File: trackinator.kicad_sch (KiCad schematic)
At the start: 2 parts, among them U6 FE2.1

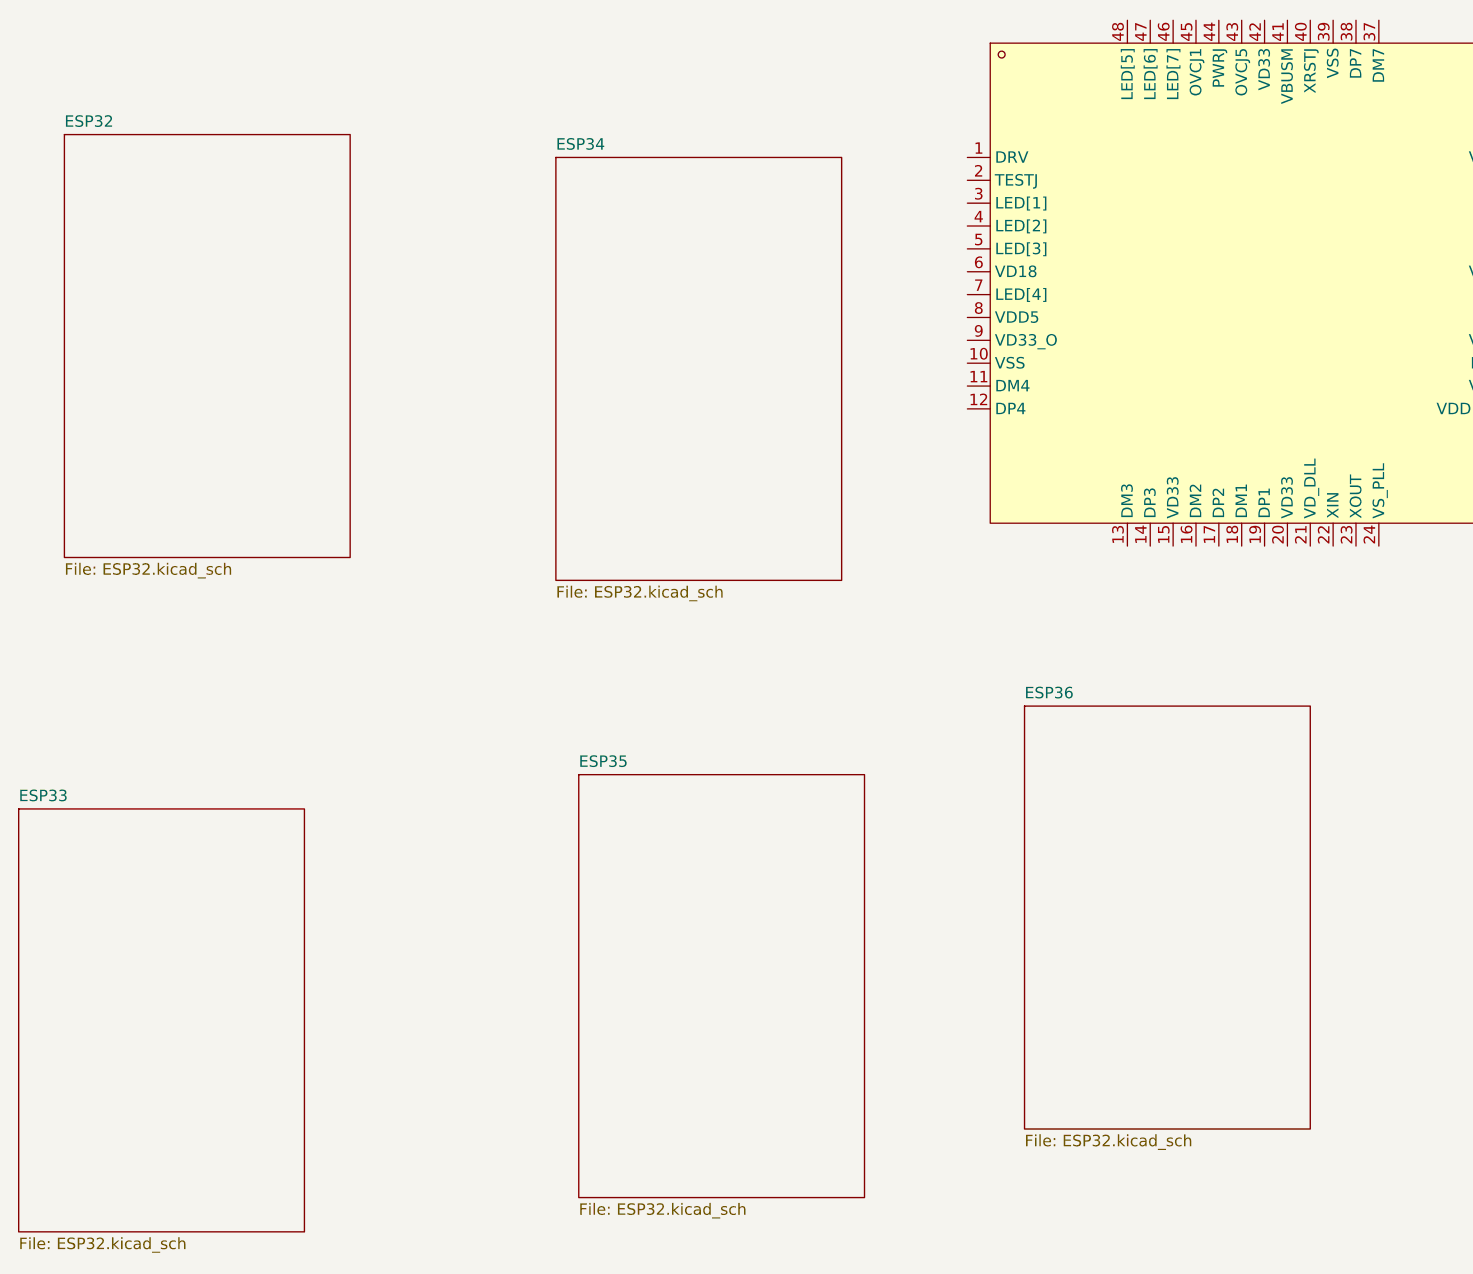
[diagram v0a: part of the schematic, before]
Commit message: FFC camera connector + pin mapping
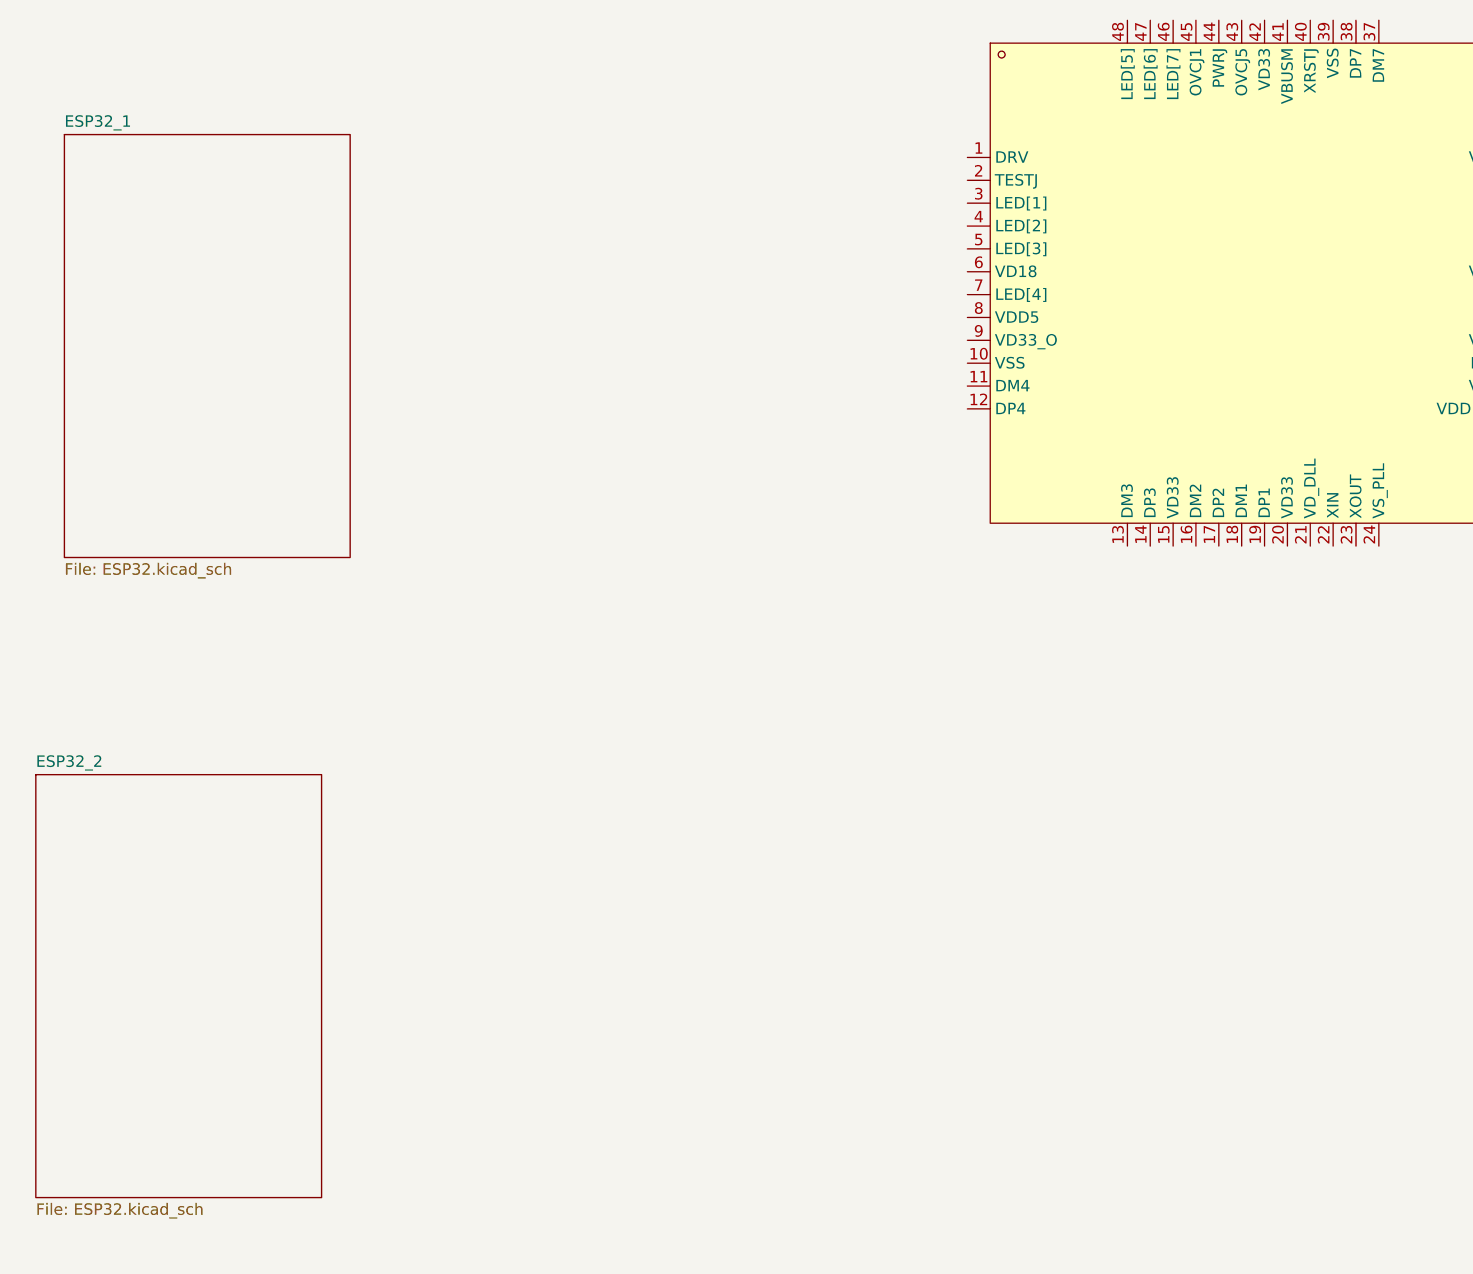
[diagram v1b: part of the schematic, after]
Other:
- sheet ESP32 renamed ESP32_1
- removed sheet ESP33
- removed sheet ESP34
- removed sheet ESP35
- removed sheet ESP36
- added sheet ESP32_2 (ESP32.kicad_sch)
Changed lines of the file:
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@@
-    )
-  )
-  (sheet (at 110.49 107.95) (size 31.75 46.99) (fields_autoplaced)
-    (stroke (width 0.1524) (type solid))
-    (fill (color 0 0 0 0.0000))
-    (property "Sheetname" "ESP35" (at 110.49 107.2384 0)
-      (effects (font (size 1.27 1.27)) (justify left bottom))
-    )
-    (property "Sheetfile" "ESP32.kicad_sch" (at 110.49 155.5246 0)
-      (effects (font (size 1.27 1.27)) (justify left top))
-    )
-    (instances
-      (project "trackinator"
-        (path "/21f69d4f-5d5e-42f8-b3db-8d41c47386dd" (page "5"))
-      )
     )
   )
@@
     (stroke (width 0.1524) (type solid))
     (fill (color 0 0 0 0.0000))
-    (property "Sheetname" "ESP32" (at 53.34 36.1184 0)
+    (property "Sheetname" "ESP32_1" (at 53.34 36.1184 0)
       (effects (font (size 1.27 1.27)) (justify left bottom))
     )
@@
     )
   )
-  (sheet (at 48.26 111.76) (size 31.75 46.99) (fields_autoplaced)
+  (sheet (at 50.165 107.95) (size 31.75 46.99) (fields_autoplaced)
     (stroke (width 0.1524) (type solid))
     (fill (color 0 0 0 0.0000))
-    (property "Sheetname" "ESP33" (at 48.26 111.0484 0)
+    (property "Sheetname" "ESP32_2" (at 50.165 107.2384 0)
       (effects (font (size 1.27 1.27)) (justify left bottom))
     )
-    (property "Sheetfile" "ESP32.kicad_sch" (at 48.26 159.3346 0)
+    (property "Sheetfile" "ESP32.kicad_sch" (at 50.165 155.5246 0)
       (effects (font (size 1.27 1.27)) (justify left top))
     )
@@
       )
     )
-  )
-  (sheet (at 107.95 39.37) (size 31.75 46.99) (fields_autoplaced)
-    (stroke (width 0.1524) (type solid))
-    (fill (color 0 0 0 0.0000))
-    (property "Sheetname" "ESP34" (at 107.95 38.6584 0)
-      (effects (font (size 1.27 1.27)) (justify left bottom))
-    )
-    (property "Sheetfile" "ESP32.kicad_sch" (at 107.95 86.9446 0)
-      (effects (font (size 1.27 1.27)) (justify left top))
-    )
-    (instances
-      (project "trackinator"
-        (path "/21f69d4f-5d5e-42f8-b3db-8d41c47386dd" (page "4"))
-      )
-    )
-  )
-  (sheet (at 160.02 100.33) (size 31.75 46.99) (fields_autoplaced)
-    (stroke (width 0.1524) (type solid))
-    (fill (color 0 0 0 0.0000))
-    (property "Sheetname" "ESP36" (at 160.02 99.6184 0)
-      (effects (font (size 1.27 1.27)) (justify left bottom))
-    )
-    (property "Sheetfile" "ESP32.kicad_sch" (at 160.02 147.9046 0)
-      (effects (font (size 1.27 1.27)) (justify left top))
-    )
-    (instances
-      (project "trackinator"
-        (path "/21f69d4f-5d5e-42f8-b3db-8d41c47386dd" (page "6"))
-      )
-    )

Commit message: revving up
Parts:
- added C1, C2: 10u, symbol Device:C
- added R2: 2k7, symbol Device:R
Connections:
- net GND: now reaches U6.10 (VSS)
- net GND: now also U6.24 (VS_PLL), U6.39 (VSS), USB1.4 (GND), USB1.5, USB1.6, C1.1, C2.1, R2.1
- net ESP32_1/USB_DN: now reaches U6.11 (DM4)
- net ESP32_1/USB_DP: now reaches U6.12 (DP4)
- net at U6.21 (VD_DLL): now also U6.28 (VD18), U6.6 (VD18)
- net at U6.25 (VDD18_O): now also C2.2
- net at U6.27 (REXT): now also R2.2
- net at U6.29 (DMU): now also USB1.2 (D-)
- net at U6.30 (DPU): now also USB1.3 (D+)
- net +5V: now reaches U6.41 (VBUSM)
- net +5V: now also U6.8 (VDD5), USB1.1 (VCC)
- net at U6.9 (VD33_O): now also C1.2
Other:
- removed sheet ESP32_2
- sheet ESP32_1 ports: added USB_DN, USB_DP; removed none
- note added: "100n Caps on all 3v3 and 1v8 pins pullup + 100n cap on XRSTJ crystal 12 Mhz crystal, caps are integrated (no idea on load capacitance) leds + resistors - don't disable/mark non-removable any ports by default - have an unpopulated footprint for resistor to ground NP footprint for an eeprom just for lols USB net class rules (and assigning signals into it)"
- moved on the sheet: USB1

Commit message: grow todo but also do a lot of work
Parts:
- added C10, C11, C12, C18, C3, C4, C5, C6, C7, C8, C9: 100n, Capacitor_SMD:C_0402_1005Metric, symbol Device:C
- added C17: 10u, Capacitor_SMD:C_0603_1608Metric, symbol Device:C
- added LED3: RED, easyeda2kicad:LED0603-RD, symbol easyeda2kicad:KT-0603R
- added R10: 1k, Resistor_SMD:R_0402_1005Metric, symbol Device:R
- added R4, R7, R8: 10k, Resistor_SMD:R_0402_1005Metric, symbol Device:R
- added SW1, SW2: TS-1187A-B-A-B, easyeda2kicad:SW-SMD_4P-L5.1-W5.1-P3.70-LS6.5-TL-2, symbol easyeda2kicad:TS-1187A-B-A-B
- added U1: M24C02-WMN, Package_SO:SOIC-8_3.9x4.9mm_P1.27mm, symbol Memory_EEPROM:M24C02-WMN
- added Y1: Crystal_GND24_Small, Crystal:Crystal_SMD_3225-4Pin_3.2x2.5mm, symbol Device:Crystal_GND24_Small
- C1, C2: footprint (none) -> Capacitor_SMD:C_0603_1608Metric
- R2: footprint (none) -> Resistor_SMD:R_0402_1005Metric
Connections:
- net GND: now also C10.1, C11.1, C12.1, C17.1, C18.1, C3.1, C4.1, C5.1, C6.1, C7.1, C8.1, C9.1, LED3.1 (K), SW1.1 (A), SW1.2 (B), SW2.1 (A), SW2.2 (B), U1.1 (E0), U1.2 (E1), U1.3 (E2), U1.4 (VSS), U1.7 (~{WC}), Y1.2, Y1.4
- net at C2.2, U6.25 (VDD18_O): now also U6.21 (VD_DLL), U6.28 (VD18), U6.6 (VD18), C10.2, C11.2, C9.2
- net Config_LED1/DRV: now reaches U6.1 (DRV)
- net Config_LED1/DRV: now also R10.2
- net +3V3: now reaches U6.15 (VD33)
- net +3V3: now also U6.20 (VD33), U6.26 (VD33), U6.31 (VD33), U6.36 (VD33), U6.42 (VD33), C18.2, C3.2, C4.2, C5.2, C6.2, C7.2, C8.2, R4.1, R7.2, R8.2, U1.8 (VCC)
- net HUB_SDA: now reaches U6.2 (TESTJ)
- net HUB_SDA: now also U1.5 (SDA)
- net at U6.22 (XIN): now also Y1.3
- net at U6.23 (XOUT): now also Y1.1
- net HUB_SCL: now reaches U6.3 (LED[1])
- net HUB_SCL: now also U1.6 (SCL)
- net Config_LED2/LED: now reaches U6.4 (LED[2])
- net at U6.40 (XRSTJ): now also C12.2, R4.2
- net Config_LED7/LED: now reaches U6.46 (LED[7])
- net Config_LED6/LED: now reaches U6.47 (LED[6])
- net Config_LED5/LED: now reaches U6.48 (LED[5])
- net Config_LED3/LED: now reaches U6.5 (LED[3])
- net Config_LED4/LED: now reaches U6.7 (LED[4])
- new net: LED3.2 (A), R10.1
- new net ESP32_1/CHIP_PU: C17.2, R8.1, SW2.3 (C), SW2.4 (D)
- new net ESP32_1/GPIO0: R7.1, SW1.3 (C), SW1.4 (D)
- no-connect marks 0 -> 3
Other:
- added sheet Config_LED1 (config_led.kicad_sch)
- added sheet Config_LED2 (config_led.kicad_sch)
- added sheet Config_LED3 (config_led.kicad_sch)
- added sheet Config_LED4 (config_led.kicad_sch)
- added sheet Config_LED5 (config_led.kicad_sch)
- added sheet Config_LED6 (config_led.kicad_sch)
- added sheet Config_LED7 (config_led.kicad_sch)
- added sheet Power (power.kicad_sch)
- sheet ESP32_1 ports: added CHIP_PU, GPIO0, MTCK, MTDI, MTDO, MTMS; removed none
- note added: "Expected EEPROM address: 0b10100000"
- note added: "The hub runs on 3v3 from a buck"
- note added: "USB net class rules (and assigning signals into it)"
- note added: "Use MLCC caps with at least 2X voltage rating to avoid DC-bias loss of capacitance"
- note removed: "100n Caps on all 3v3 and 1v8 pins pullup + 100n cap on XRSTJ crystal 12 Mhz crystal, caps are integrated (no idea on load capacitance) leds + resistors - don't disable/mark non-removable any ports by default - have an unpopulated footprint for resistor to ground NP footprint for an eeprom just for lols USB net class rules (and assigning signals into it)"
- moved on the sheet: R2

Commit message: crystals and drivers
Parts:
- added C35, C36, C37: 100n, Capacitor_SMD:C_0402_1005Metric, symbol Device:C
- added J1: Conn_01x04_Pin, symbol Connector:Conn_01x04_Pin
- added U5, U7, U8: SP3481EN, Package_SO:SOIC-8_3.9x4.9mm_P1.27mm, symbol Interface_UART:SP3481EN
- Y1: value Crystal_GND24_Small -> 12Mhz
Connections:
- net +5V: now also C35.2, C36.2, C37.2, U5.8 (VCC), U7.8 (VCC), U8.8 (VCC)
- net GND: now also C35.1, C36.1, C37.1, U5.5 (GND), U7.5 (GND), U8.5 (GND)
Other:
- sheet ESP32_1 ports: added E_CLK; removed none
- note added: "Add some pin headers"
- note added: "GND 5V TACH PWM"
- note added: "I declare this a motor driver"
- note added: "Series resistor going from the ESP32 to WS2812B"
- moved on the sheet: Y1
